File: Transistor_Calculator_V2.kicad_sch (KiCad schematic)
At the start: 51 parts, among them J1 5V, J2 GND, Q1 2N3904, Q10 2N3904, Q11 2N3904, Q12 2N3904, Q13 2N3904, Q14 2N3904, Q15 2N3904, Q16 2N3904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

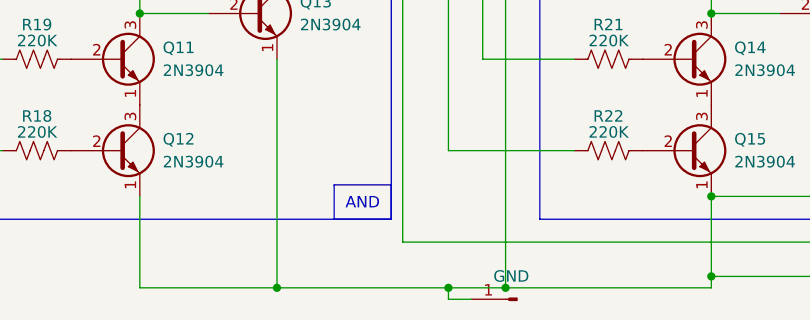
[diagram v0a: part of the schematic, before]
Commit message: update transistors
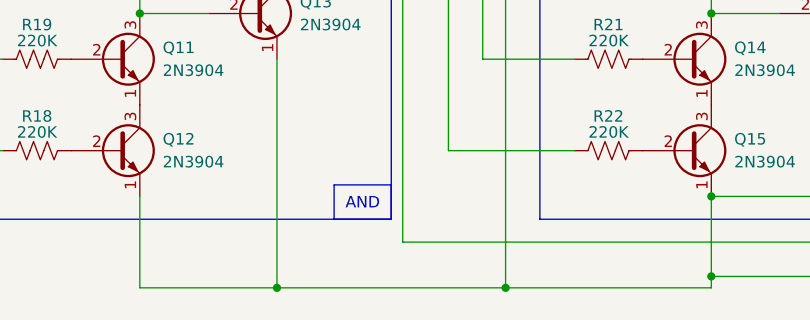
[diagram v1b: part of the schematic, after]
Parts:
- removed J2: GND, Connector_Pin:Pin_D1.0mm_L10.0mm_LooseFit, symbol Connector:Conn_01x01_Pin
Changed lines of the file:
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@@
 	)
 	(junction
-		(at 92.71 193.04)
-		(diameter 0)
-		(color 0 0 0 0)
-	)
-	(junction
 		(at 137.16 157.48)
 		(diameter 0)
@@
 	(wire
 		(pts
-			(xy 92.71 193.04) (xy 99.06 193.04)
-		)
-		(stroke
-			(width 0)
-			(type default)
-		)
-	)
-	(wire
-		(pts
-			(xy 73.66 193.04) (xy 92.71 193.04)
+			(xy 73.66 193.04) (xy 99.06 193.04)
 		)
 		(stroke
@@
 	(wire
 		(pts
-			(xy 92.71 194.31) (xy 92.71 193.04)
-		)
-		(stroke
-			(width 0)
-			(type default)
-		)
-	)
-	(wire
-		(pts
 			(xy 143.51 144.78) (xy 152.4 144.78)
 		)
@@
 	(wire
 		(pts
-			(xy 95.25 194.31) (xy 92.71 194.31)
-		)
-		(stroke
-			(width 0)
-			(type default)
-		)
-	)
-	(wire
-		(pts
 			(xy 22.86 102.87) (xy 29.21 102.87)
 		)
@@
 					(unit 1)
 				)
-			)
-		)
-	)
-	(symbol
-		(lib_id "Connector:Conn_01x01_Pin")
-		(at 100.33 194.31 180)
-		(unit 1)
-		(exclude_from_sim no)
-		(in_bom yes)
-		(on_board yes)
-		(dnp no)
-		(fields_autoplaced yes)
-		(property "Reference" "J2"
-			(at 99.695 189.23 0)
-			(effects
-				(font
-					(size 1.27 1.27)
-				)
-				(hide yes)
-			)
-		)
-		(property "Value" "GND"
-			(at 99.695 191.77 0)
-			(effects
-				(font
-					(size 1.27 1.27)
-				)
-			)
-		)
-		(property "Footprint" "Connector_Pin:Pin_D1.0mm_L10.0mm_LooseFit"
-			(at 100.33 194.31 0)
-			(effects
-				(font
-					(size 1.27 1.27)
-				)
-				(hide yes)
-			)
-		)
-		(property "Datasheet" "~"
-			(at 100.33 194.31 0)
-			(effects
-				(font
-					(size 1.27 1.27)
-				)
-				(hide yes)
-			)
-		)
-		(property "Description" "Generic connector, single row, 01x01, script generated"
-			(at 100.33 194.31 0)
-			(effects
-				(font
-					(size 1.27 1.27)
-				)
-				(hide yes)
-			)
-		)
-		(pin "1"
-		)
-		(instances
-			(project "Transistor_Calculator_V2"
-				(path "/4e74c2aa-3410-4407-95d8-73d62854742b"
-					(reference "J2")
-					(unit 1)
-				)

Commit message: update transistors
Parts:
- removed J1: 5V, Connector_Pin:Pin_D1.0mm_L10.0mm_LooseFit, symbol Connector:Conn_01x01_Pin
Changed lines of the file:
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@@
-	)
-	(junction
-		(at 113.03 31.75)
-		(diameter 0)
-		(color 0 0 0 0)
 	)
 	(junction
@@
 	(wire
 		(pts
-			(xy 107.95 31.75) (xy 113.03 31.75)
+			(xy 107.95 31.75) (xy 121.92 31.75)
 		)
 		(stroke
@@
 	(wire
 		(pts
-			(xy 113.03 31.75) (xy 121.92 31.75)
-		)
-		(stroke
-			(width 0)
-			(type default)
-		)
-	)
-	(wire
-		(pts
 			(xy 127 72.39) (xy 146.05 72.39)
 		)
@@
 		(pts
 			(xy 29.21 177.8) (xy 29.21 102.87)
-		)
-		(stroke
-			(width 0)
-			(type default)
-		)
-	)
-	(wire
-		(pts
-			(xy 113.03 24.13) (xy 113.03 31.75)
 		)
 		(stroke
@@
 					(unit 1)
 				)
-			)
-		)
-	)
-	(symbol
-		(lib_id "Connector:Conn_01x01_Pin")
-		(at 118.11 24.13 180)
-		(unit 1)
-		(exclude_from_sim no)
-		(in_bom yes)
-		(on_board yes)
-		(dnp no)
-		(fields_autoplaced yes)
-		(property "Reference" "J1"
-			(at 117.475 19.05 0)
-			(effects
-				(font
-					(size 1.27 1.27)
-				)
-			)
-		)
-		(property "Value" "5V"
-			(at 117.475 21.59 0)
-			(effects
-				(font
-					(size 1.27 1.27)
-				)
-			)
-		)
-		(property "Footprint" "Connector_Pin:Pin_D1.0mm_L10.0mm_LooseFit"
-			(at 118.11 24.13 0)
-			(effects
-				(font
-					(size 1.27 1.27)
-				)
-				(hide yes)
-			)
-		)
-		(property "Datasheet" "~"
-			(at 118.11 24.13 0)
-			(effects
-				(font
-					(size 1.27 1.27)
-				)
-				(hide yes)
-			)
-		)
-		(property "Description" "Generic connector, single row, 01x01, script generated"
-			(at 118.11 24.13 0)
-			(effects
-				(font
-					(size 1.27 1.27)
-				)
-				(hide yes)
-			)
-		)
-		(pin "1"
-		)
-		(instances
-			(project "Transistor_Calculator_V2"
-				(path "/4e74c2aa-3410-4407-95d8-73d62854742b"
-					(reference "J1")
-					(unit 1)
-				)

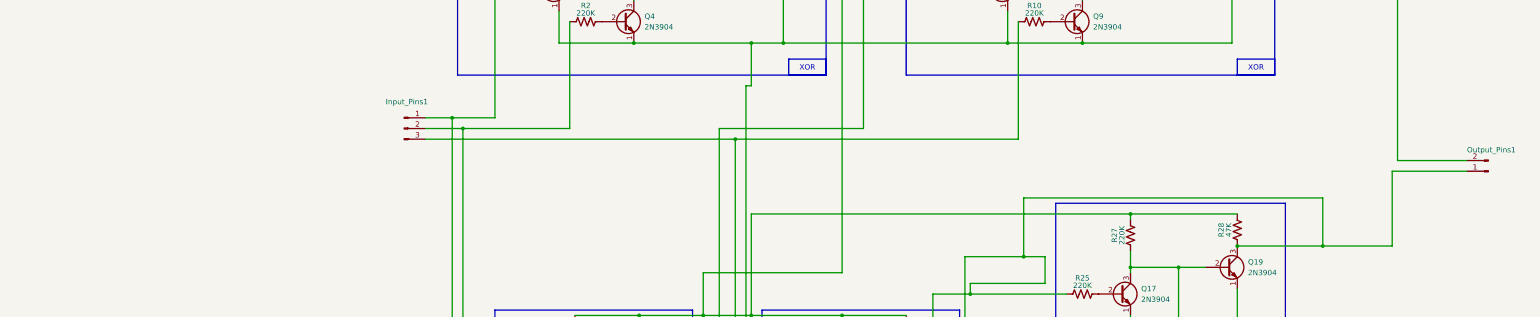
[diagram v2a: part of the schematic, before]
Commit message: update transistors
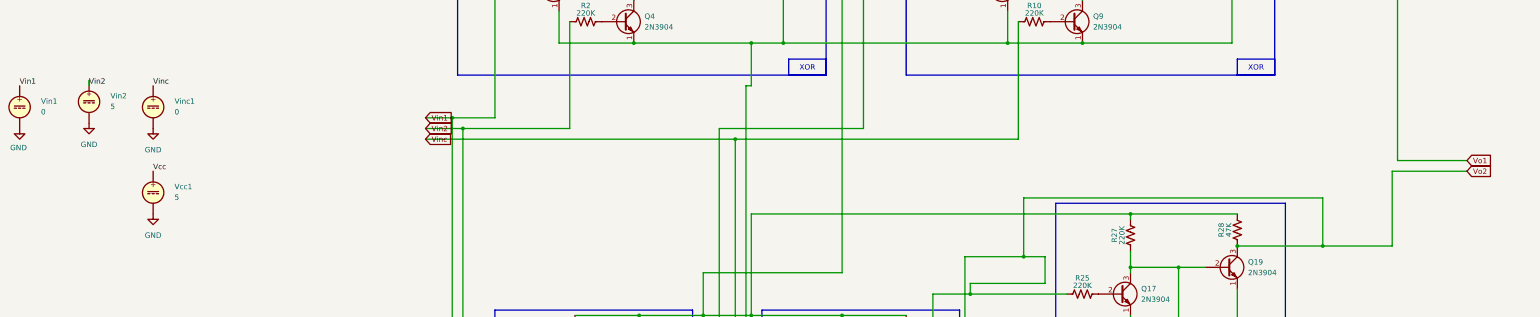
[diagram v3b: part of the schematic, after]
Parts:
- removed Input_Pins1: ~, Connector_Wire:SolderWire-0.5sqmm_1x03_P4.6mm_D0.9mm_OD2.1mm, symbol Connector:Conn_01x03_Pin
- removed Output_Pins1: ~, Connector_Wire:SolderWire-0.5sqmm_1x02_P4.6mm_D0.9mm_OD2.1mm, symbol Connector:Conn_01x02_Pin
- added Vcc1, Vin2: 5, symbol Simulation_SPICE:VDC
- added Vin1, Vinc1: 0, symbol Simulation_SPICE:VDC
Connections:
- net Vo2: now reaches Q13.3 (C), Q16.3 (C), Q19.3 (C), R16.1, R24.1, R25.1, R26.1, R28.1
- net Vo1: now reaches Q10.3 (C), R8.1
- net Vin1: now reaches R1.1, R18.1
- net Vin1: now also Vin1.1
- net Vinc: now reaches R10.1, R21.1
- net Vinc: now also Vinc1.1
- net Vin2: now reaches R19.1, R2.1
- net Vin2: now also Vin2.1
- new net GND: Vcc1.2, Vin1.2, Vin2.2, Vinc1.2
- new net Vcc: Vcc1.1
